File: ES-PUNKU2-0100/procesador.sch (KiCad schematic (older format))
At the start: 23 parts

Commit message: Correcciones al esquemático. Asignación de referencias y valores. Actualización de Librerías.
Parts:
- removed D?: LS4148, symbol Device:D
- removed U?: LM2575S5, encapsulados:D2PAK_TO-263_5Patas, symbol Regulator_Switching:LM2575-5.0BU
- added D1: SK210TR, encapsulados:DO-214AA, symbol Device:D_Schottky_ALT
- added D4: CD-MBL206SL, encapsulados:BOURNS-0.23x0.20, symbol componentes:Diode_Bridge
- added U1: LM2575, encapsulados:D2PAK_TO-263_5Patas, symbol componentes:LM2575
- BT1: renamed from BT?; footprint (none) -> encapsulados:CR2032_Horizontal
- C2, C5, C7: renamed from C?; footprint (none) -> encapsulados:C_1206_0805_Dual
- D2: renamed from D?; DigiKey (none) -> 1655-1584-1-ND
- J3: renamed from J?; footprint (none) -> encapsulados:Pin_Header_Straight_1x02_Pitch2.54mm
- J4: renamed from J?; footprint (none) -> encapsulados:SD_AMPHENOL_114_00841_68; DigiKey (none) -> 114-00841-68-1-ND
- L1: renamed from L?; footprint encapsulados:Choke_Radial_8mm_0,7mm-Drills -> encapsulados:BOURNS_INDUCTOR_SRR1260; DigiKey (none) -> SRR1280-331KLCT-ND
- R1: renamed from R?; footprint (none) -> encapsulados:R_1206_0805_Dual
- SW1: renamed from SW?; footprint (none) -> encapsulados:TACT_SWITCH
- U2: renamed from U?; footprint MODULE_ESP32-WROOM-32D -> encapsulados:MODULE_ESP32-WROOM-32D; DigiKey (none) -> 1904-1023-1-ND; Digikey 1904-1023-1-ND -> (none)
- U4: renamed from U?; footprint (none) -> encapsulados:SOIC-8; DigiKey (none) -> MCP7940NT-I/SNCT-ND
- Y1: renamed from Y?; footprint (none) -> encapsulados:CRISTAL_EPSON_3,2mm_1,5mm; DigiKey (none) -> SER4089CT-ND
- gave numbers to parts that had none: 8
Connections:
- wire segments 139 -> 147
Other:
- moved on the sheet: BT1, C1, C3, C4, C6, C7, D2, J2, L1, R1, U3, U4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

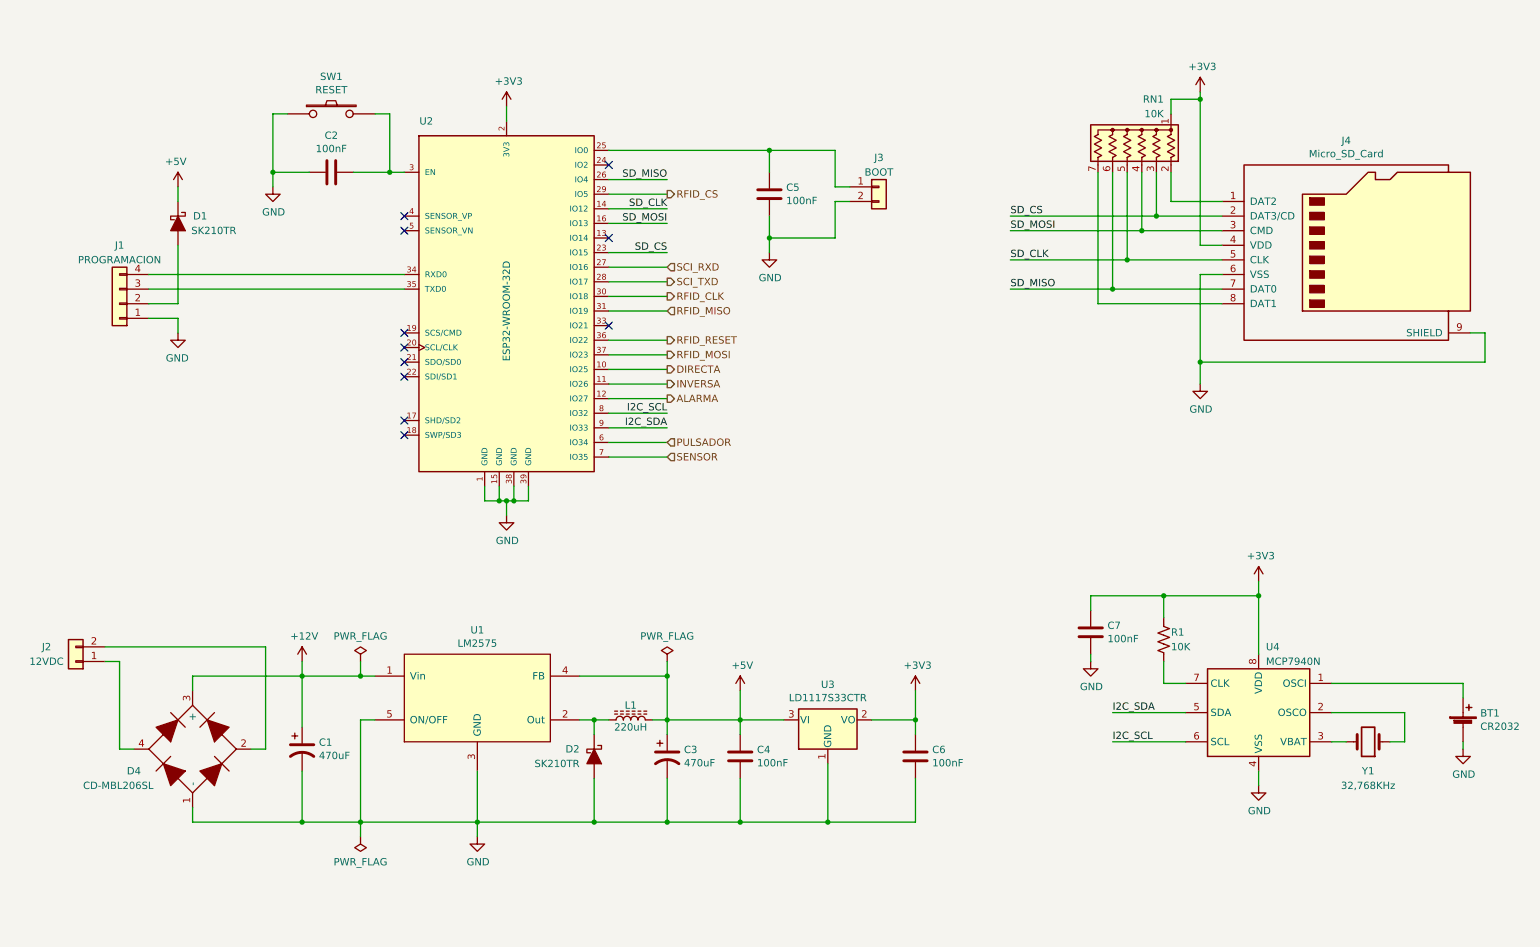
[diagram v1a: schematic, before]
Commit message: Incorporación de las correcciones sugeridas por Martin Ribelotta y posicionamiento de componentes
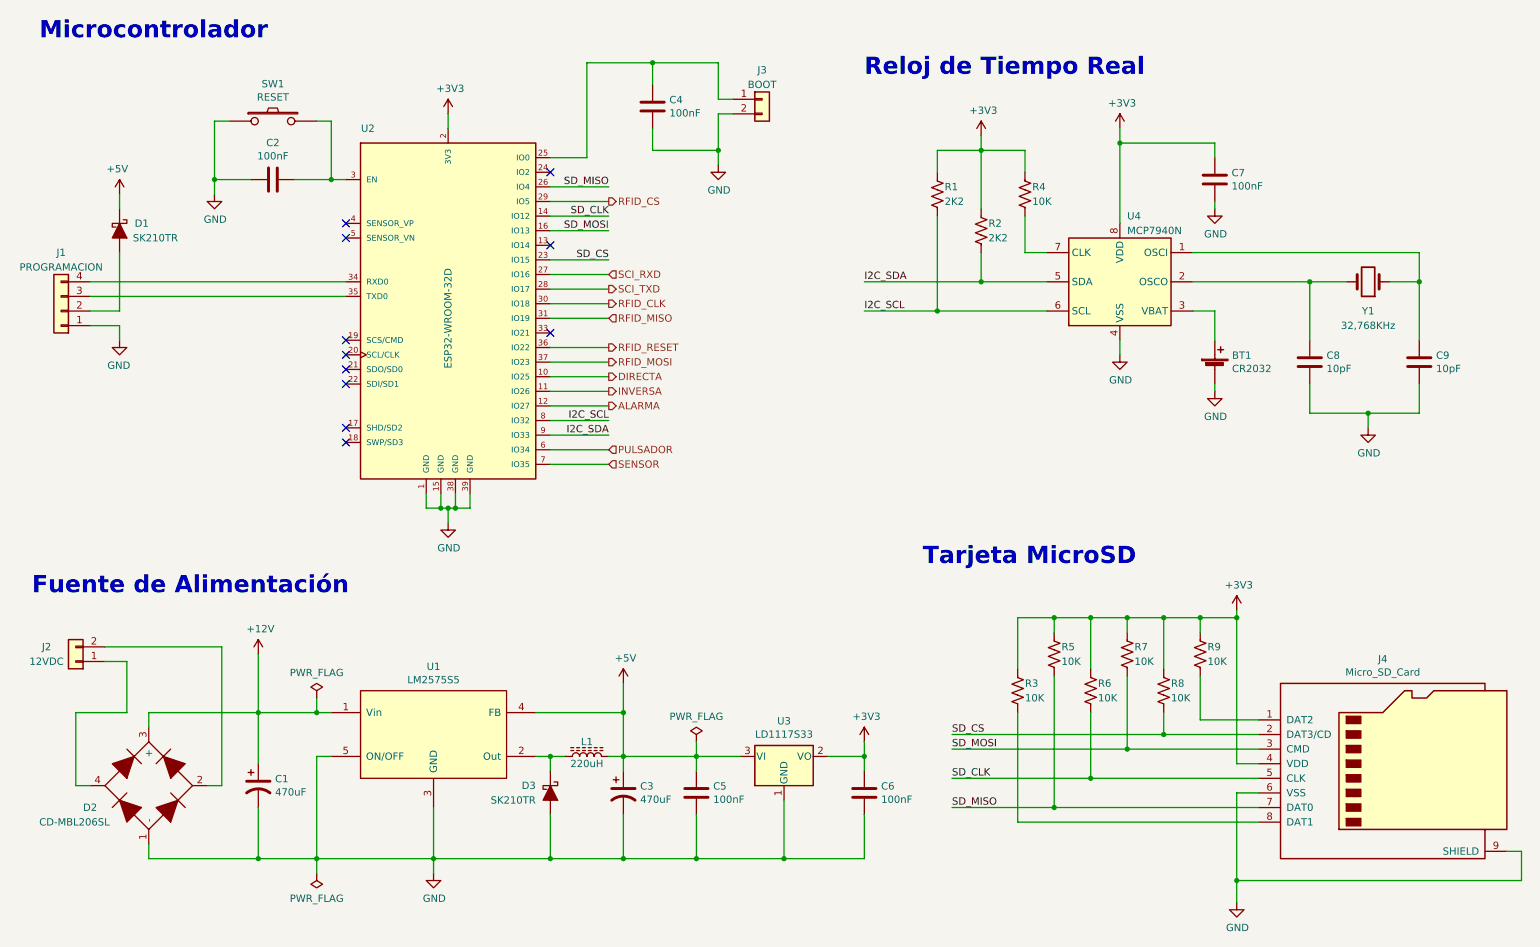
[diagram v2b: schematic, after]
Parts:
- removed RN1: 10K, Resistor_THT:R_Array_SIP7, symbol Device:R_Network06_US
- added C8, C9: 10pF, encapsulados:C_1206_0805_Dual, symbol Device:C
- added R1, R2: 2K2, encapsulados:R_1206_0805_Dual, symbol Device:R_US
- added R3, R5, R6, R7, R8, R9: 10K, encapsulados:R_1206_0805_Dual, symbol Device:R_US
- BT1: footprint encapsulados:CR2032_Horizontal -> encapsulados:BatteryHolder_Keystone_1058_1x2032; Codigo (none) -> 1058; DigiKey (none) -> 36-1058-ND; Fabricante (none) -> Keystone electronics
- C1, C3: footprint encapsulados:CP_Radial_D10_L20_P5 -> encapsulados:CP_Elec_8x10
- D1: Codigo (none) -> SK210TR; Fabricante (none) -> SMC Diode Solutions
- D2: renamed from D4; Codigo (none) -> CD-MBL206SL; Fabricante (none) -> Bourns Inc.
- D3: renamed from D2; Codigo (none) -> SK210TR; Fabricante (none) -> SMC Diode Solutions
- U1: value LM2575 -> LM2575S5; Codigo (none) -> LM2575S-5.0/NOPB; DigiKey (none) -> LM2575S-5.0/NOPB-ND; Fabricante (none) -> Texas Instruments
- U2: Codigo (none) -> ESP32-WROOM-32D; Fabricante (none) -> Espressif Systems
- U3: value LD1117S33CTR -> LD1117S33; Codigo (none) -> LD1117S33CTR; DigiKey (none) -> 497-1241-1-ND; Fabricante (none) -> STMicroelectronics
- U4: Codigo (none) -> MCP7940NT-I/SN; Fabricante (none) -> Microchip Technology
- Y1: Codigo (none) -> FC-135 32.768KA-AG0; Fabricante (none) -> Epson
- renumbered C5 to C4, C4 to C5, R1 to R4
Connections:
- net +3V3: now also R1.1, R2.1, R3.1, R5.1, R6.1, R7.1, R8.1, R9.1
- net GND: now also C8.2, C9.2
- net I2C_SCL: now also R1.2
- net I2C_SDA: now also R2.2
- net SD_CLK: now also R6.2
- net SD_CS: now also R8.2
- net SD_MISO: now also R5.2
- net SD_MOSI: now also R7.2
- net at U4.1 (OSCI): now also Y1.1, C9.1; no longer BT1.1 (+)
- net at U4.2 (OSCO): now also Y1.2, C8.1; no longer Y1.1
- net at U4.3 (VBAT): now also BT1.1 (+); no longer Y1.2
- net at J4.1 (DAT2): now also R9.2
- net at J4.8 (DAT1): now also R3.2
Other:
- note added: "Fuente de Alimentación"
- note added: "Microcontrolador"
- note added: "Reloj de Tiempo Real"
- note added: "Tarjeta MicroSD"
- moved on the sheet: BT1, C1, C2, C3, C4, C5, C6, C7, D1, D2, D3, J1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

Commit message: Primera versión ruteada de la placa
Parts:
- removed SW1: RESET, encapsulados:TACT_SWITCH, symbol componentes:SW_PUSH
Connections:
- net ALARMA: now also U2.8 (IO32); no longer U2.12 (IO27)
- net DIRECTA: now also U2.7 (IO35); no longer U2.10 (IO25)
- net GND: now also C2.1; no longer C2.2, J4.9 (SHIELD)
- net I2C_SCL: now also U2.12 (IO27); no longer U2.8 (IO32)
- net I2C_SDA: now also U2.11 (IO26); no longer U2.9 (IO33)
- net INVERSA: now also U2.6 (IO34); no longer U2.11 (IO26)
- net PULSADOR: now also U2.9 (IO33); no longer U2.6 (IO34)
- net SENSOR: now also U2.10 (IO25); no longer U2.7 (IO35)
- net at U2.3 (EN): now also C2.2; no longer C2.1
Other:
- moved on the sheet: BT1, C1, C2, C3, C4, C5, C6, C7, C8, C9, D1, D2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

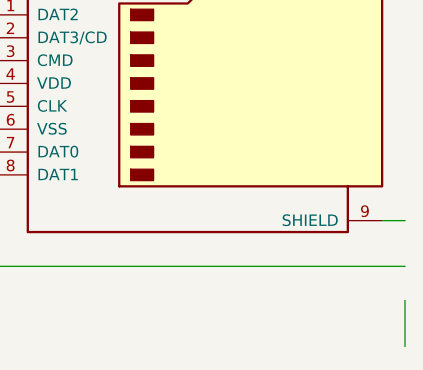
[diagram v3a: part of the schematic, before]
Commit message: Correcciones de ruteo y agregado de una protección para la salida del puente H
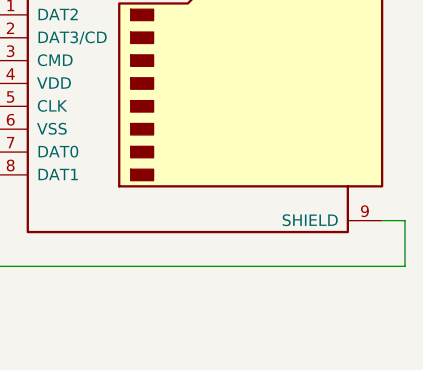
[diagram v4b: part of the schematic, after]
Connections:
- net GND: now also J4.9 (SHIELD)
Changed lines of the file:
@@
 	10850 6200 10950 6200
-Wire Wire Line
-	10950 6550 10950 6750
 Wire Wire Line
 	10950 6400 9000 6400
@@
 	1    0    0    -1
 $EndComp
+Wire Wire Line
+	10950 6200 10950 6400
 $EndSCHEMATC
